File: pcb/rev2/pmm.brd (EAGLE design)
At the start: 78.6 x 43 mm, 48 parts, among them IC3 STM32F042F4, J1 AUDIO_JACK_3.5MM_PTH, J2 FFC3B07-05-T, SW4 324_SW, U2 USBC_16P, U4 XC6206_DEV

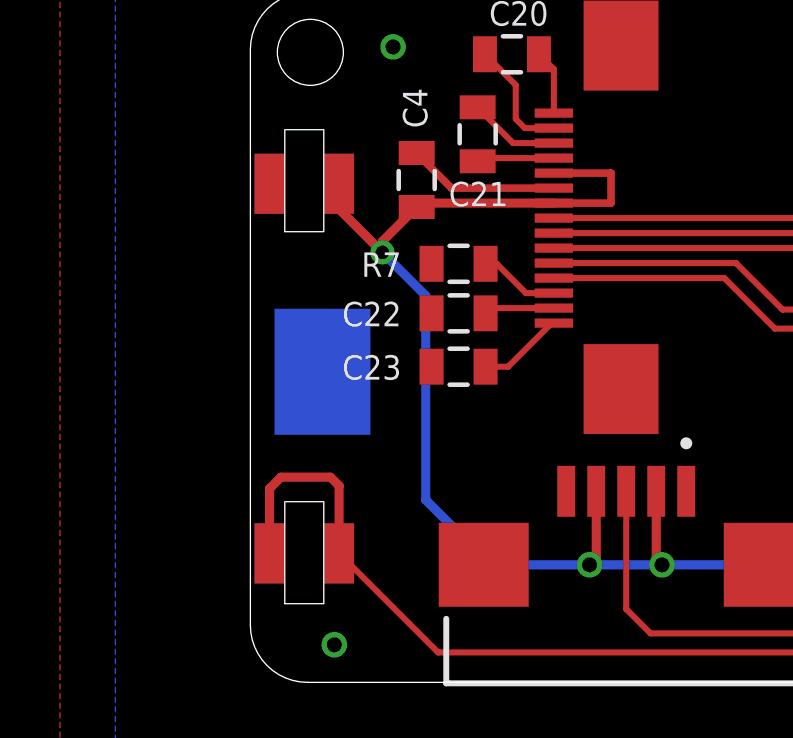
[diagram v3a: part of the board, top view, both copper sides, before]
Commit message: adjusted for pcb thickness
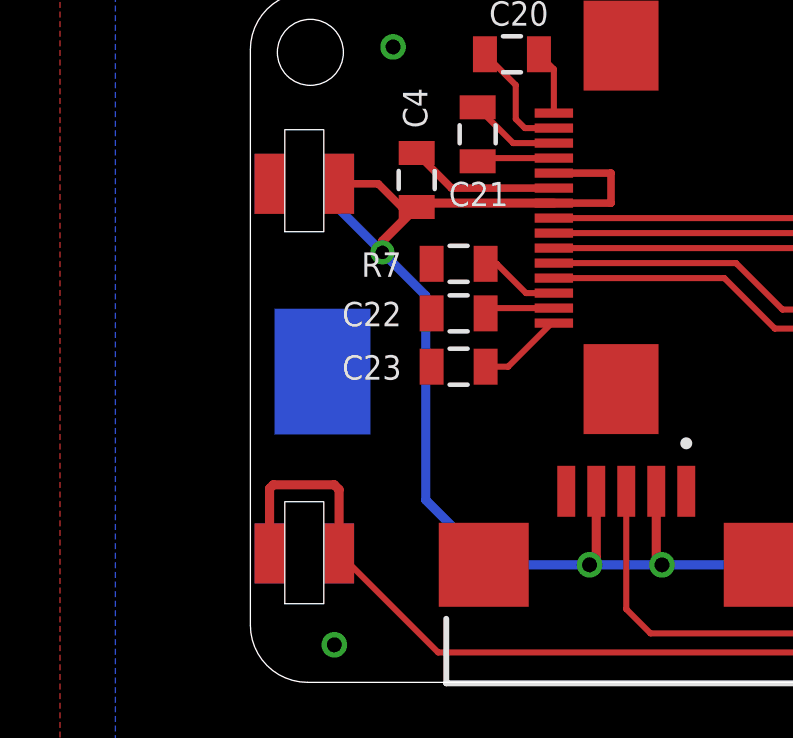
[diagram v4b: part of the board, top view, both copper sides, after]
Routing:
- net +3V3: track 143.9 -> 144.8 mm
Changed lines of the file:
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@@
 <setting verticaltext="up"/>
 </settings>
-<grid distance="10" unitdist="mil" unit="mil" style="lines" multiple="1" display="no" altdistance="1" altunitdist="mil" altunit="mil"/>
+<grid distance="5" unitdist="mil" unit="mil" style="lines" multiple="1" display="no" altdistance="1" altunitdist="mil" altunit="mil"/>
 <layers>
 <layer number="1" name="Top" color="4" fill="1" visible="yes" active="yes"/>
@@
 <layer number="19" name="Unrouted" color="6" fill="1" visible="yes" active="yes"/>
 <layer number="20" name="Dimension" color="24" fill="1" visible="yes" active="yes"/>
-<layer number="21" name="tPlace" color="7" fill="1" visible="yes" active="yes"/>
-<layer number="22" name="bPlace" color="7" fill="1" visible="yes" active="yes"/>
+<layer number="21" name="tPlace" color="7" fill="1" visible="no" active="yes"/>
+<layer number="22" name="bPlace" color="7" fill="1" visible="no" active="yes"/>
 <layer number="23" name="tOrigins" color="15" fill="1" visible="yes" active="yes"/>
 <layer number="24" name="bOrigins" color="15" fill="1" visible="yes" active="yes"/>
-<layer number="25" name="tNames" color="7" fill="1" visible="yes" active="yes"/>
-<layer number="26" name="bNames" color="7" fill="1" visible="yes" active="yes"/>
-<layer number="27" name="tValues" color="7" fill="1" visible="yes" active="yes"/>
-<layer number="28" name="bValues" color="7" fill="1" visible="yes" active="yes"/>
+<layer number="25" name="tNames" color="7" fill="1" visible="no" active="yes"/>
+<layer number="26" name="bNames" color="7" fill="1" visible="no" active="yes"/>
+<layer number="27" name="tValues" color="7" fill="1" visible="no" active="yes"/>
+<layer number="28" name="bValues" color="7" fill="1" visible="no" active="yes"/>
 <layer number="29" name="tStop" color="7" fill="3" visible="no" active="yes"/>
 <layer number="30" name="bStop" color="7" fill="6" visible="no" active="yes"/>
@@
 <layer number="49" name="Reference" color="7" fill="1" visible="no" active="yes"/>
 <layer number="50" name="dxf" color="7" fill="1" visible="no" active="no"/>
-<layer number="51" name="tDocu" color="7" fill="1" visible="yes" active="yes"/>
-<layer number="52" name="bDocu" color="7" fill="1" visible="yes" active="yes"/>
+<layer number="51" name="tDocu" color="7" fill="1" visible="no" active="yes"/>
+<layer number="52" name="bDocu" color="7" fill="1" visible="no" active="yes"/>
 <layer number="53" name="tGND_GNDA" color="7" fill="1" visible="no" active="no"/>
 <layer number="54" name="bGND_GNDA" color="7" fill="1" visible="no" active="no"/>
@@
 <text x="13.6402" y="-23.6406" size="1.016" layer="26" rot="MR0" align="center">3</text>
 <text x="17.8312" y="-21.9896" size="1.016" layer="26" rot="MR0" align="center">LS</text>
+<polygon width="0.1524" layer="41">
+<vertex x="-31.496" y="-17.907"/>
+<vertex x="-27.432" y="-17.907"/>
+<vertex x="-27.432" y="-22.733"/>
+<vertex x="-31.496" y="-22.733"/>
+</polygon>
+<polygon width="0.1524" layer="42">
+<vertex x="-31.496" y="-18.796"/>
+<vertex x="-27.559" y="-18.796"/>
+<vertex x="-27.559" y="-22.606"/>
+<vertex x="-31.496" y="-22.606"/>
+</polygon>
 </plain>
 <attributes>
@@
 <wire x1="7.771" y1="-21.844" x2="13.589" y2="-21.844" width="0.3048" layer="16"/>
 <wire x1="-28.5432" y1="-9.2238" x2="-28.5432" y2="-8.382" width="0.3048" layer="1"/>
-<wire x1="-27.099" y1="-10.668" x2="-28.5432" y2="-9.2238" width="0.3048" layer="1"/>
 <wire x1="-27.099" y1="-10.668" x2="-27.099" y2="-10.298" width="0.3048" layer="1"/>
 <wire x1="-27.099" y1="-10.298" x2="-25.956" y2="-9.155" width="0.3048" layer="1"/>
 <wire x1="-28.5432" y1="-8.382" x2="-28.5432" y2="-9.2238" width="0.3048" layer="16"/>
 <wire x1="-28.5432" y1="-9.2238" x2="-27.099" y2="-10.668" width="0.3048" layer="16"/>
+<wire x1="-25.956" y1="-9.155" x2="-26.464" y2="-9.155" width="0.254" layer="1"/>
+<wire x1="-26.464" y1="-9.155" x2="-27.237" y2="-8.382" width="0.254" layer="1"/>
+<wire x1="-27.237" y1="-8.382" x2="-28.5432" y2="-8.382" width="0.254" layer="1"/>
 </signal>
 <signal name="USB_DP">
@@
 <wire x1="19.05" y1="-23.241" x2="20.447" y2="-21.844" width="0.2032" layer="1"/>
 <wire x1="-30.861" y1="-20.701" x2="-30.861" y2="-18.542" width="0.3048" layer="1"/>
-<wire x1="-30.861" y1="-18.542" x2="-30.48" y2="-18.161" width="0.3048" layer="1"/>
-<wire x1="-30.48" y1="-18.161" x2="-28.829" y2="-18.161" width="0.3048" layer="1"/>
-<wire x1="-28.5432" y1="-18.4468" x2="-28.5432" y2="-20.701" width="0.3048" layer="1"/>
-<wire x1="-28.829" y1="-18.161" x2="-28.5432" y2="-18.4468" width="0.3048" layer="1"/>
+<wire x1="-30.861" y1="-18.542" x2="-30.734" y2="-18.415" width="0.3048" layer="1"/>
+<wire x1="-30.734" y1="-18.415" x2="-28.702" y2="-18.415" width="0.3048" layer="1"/>
+<wire x1="-28.5432" y1="-18.5738" x2="-28.5432" y2="-20.701" width="0.3048" layer="1"/>
+<wire x1="-28.702" y1="-18.415" x2="-28.5432" y2="-18.5738" width="0.3048" layer="1"/>
 <wire x1="-25.2412" y1="-24.003" x2="-28.5432" y2="-20.701" width="0.2032" layer="1"/>
 <wire x1="-1.651" y1="-24.003" x2="-25.2412" y2="-24.003" width="0.2032" layer="1"/>

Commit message: reset button
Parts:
- added SW3: 324_SW324_SWITCH_FOOT_HOLE, 3pos_slide_switch:342_SWICH_FOOT_HOLE
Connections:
- removed net BUTTON1: IC3.4
- new net RESET: IC3.4, SW3.P$1, SW3.P$4
- net GND: now also SW3.P$2, SW3.P$3
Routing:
- net RESET: track 0.00 -> 14.7 mm, vias 0 -> 1
- net +3V3: track 144.8 -> 143.8 mm
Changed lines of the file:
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@@
 <layer number="19" name="Unrouted" color="6" fill="1" visible="yes" active="yes"/>
 <layer number="20" name="Dimension" color="24" fill="1" visible="yes" active="yes"/>
-<layer number="21" name="tPlace" color="7" fill="1" visible="no" active="yes"/>
-<layer number="22" name="bPlace" color="7" fill="1" visible="no" active="yes"/>
+<layer number="21" name="tPlace" color="7" fill="1" visible="yes" active="yes"/>
+<layer number="22" name="bPlace" color="7" fill="1" visible="yes" active="yes"/>
 <layer number="23" name="tOrigins" color="15" fill="1" visible="yes" active="yes"/>
 <layer number="24" name="bOrigins" color="15" fill="1" visible="yes" active="yes"/>
-<layer number="25" name="tNames" color="7" fill="1" visible="no" active="yes"/>
-<layer number="26" name="bNames" color="7" fill="1" visible="no" active="yes"/>
-<layer number="27" name="tValues" color="7" fill="1" visible="no" active="yes"/>
-<layer number="28" name="bValues" color="7" fill="1" visible="no" active="yes"/>
+<layer number="25" name="tNames" color="7" fill="1" visible="yes" active="yes"/>
+<layer number="26" name="bNames" color="7" fill="1" visible="yes" active="yes"/>
+<layer number="27" name="tValues" color="7" fill="1" visible="yes" active="yes"/>
+<layer number="28" name="bValues" color="7" fill="1" visible="yes" active="yes"/>
 <layer number="29" name="tStop" color="7" fill="3" visible="no" active="yes"/>
 <layer number="30" name="bStop" color="7" fill="6" visible="no" active="yes"/>
@@
 <layer number="42" name="bRestrict" color="1" fill="10" visible="yes" active="yes"/>
 <layer number="43" name="vRestrict" color="2" fill="10" visible="no" active="yes"/>
-<layer number="44" name="Drills" color="7" fill="1" visible="no" active="yes"/>
-<layer number="45" name="Holes" color="7" fill="1" visible="no" active="yes"/>
+<layer number="44" name="Drills" color="7" fill="1" visible="yes" active="yes"/>
+<layer number="45" name="Holes" color="7" fill="1" visible="yes" active="yes"/>
 <layer number="46" name="Milling" color="3" fill="1" visible="yes" active="yes"/>
 <layer number="47" name="Measures" color="7" fill="1" visible="no" active="yes"/>
@@
 <layer number="49" name="Reference" color="7" fill="1" visible="no" active="yes"/>
 <layer number="50" name="dxf" color="7" fill="1" visible="no" active="no"/>
-<layer number="51" name="tDocu" color="7" fill="1" visible="no" active="yes"/>
-<layer number="52" name="bDocu" color="7" fill="1" visible="no" active="yes"/>
+<layer number="51" name="tDocu" color="7" fill="1" visible="yes" active="yes"/>
+<layer number="52" name="bDocu" color="7" fill="1" visible="yes" active="yes"/>
 <layer number="53" name="tGND_GNDA" color="7" fill="1" visible="no" active="no"/>
 <layer number="54" name="bGND_GNDA" color="7" fill="1" visible="no" active="no"/>
@@
 <layer number="154" name="FabDoc2" color="7" fill="1" visible="no" active="yes"/>
 <layer number="155" name="FabDoc3" color="7" fill="1" visible="no" active="yes"/>
+<layer number="156" name="gesam-Maß" color="7" fill="1" visible="no" active="yes"/>
+<layer number="157" name="FaceMchng" color="7" fill="1" visible="no" active="yes"/>
+<layer number="158" name="FaceMMeas" color="7" fill="1" visible="no" active="yes"/>
+<layer number="159" name="Geh-Bear2" color="7" fill="1" visible="no" active="yes"/>
+<layer number="160" name="O_Dim" color="7" fill="1" visible="no" active="yes"/>
+<layer number="161" name="tomplace2" color="7" fill="1" visible="no" active="yes"/>
 <layer number="166" name="AntennaArea" color="7" fill="1" visible="no" active="yes"/>
 <layer number="168" name="4mmHeightArea" color="7" fill="1" visible="no" active="yes"/>
@@
 <layer number="250" name="Descript" color="3" fill="1" visible="no" active="no"/>
 <layer number="251" name="SMDround" color="12" fill="11" visible="no" active="no"/>
+<layer number="252" name="BR-BS" color="7" fill="1" visible="no" active="yes"/>
 <layer number="253" name="Extra" color="7" fill="1" visible="no" active="yes"/>
 <layer number="254" name="cooling" color="7" fill="1" visible="no" active="yes"/>
@@
 <text x="4.953" y="0.889" size="1.27" layer="25" rot="R270" align="center">HSHOE</text>
 <text x="2.3944" y="-0.1782" size="1.27" layer="25" rot="R270" align="center">GND</text>
-<text x="-5.6638" y="-23.5136" size="1.9304" layer="25" align="center">USER</text>
+<text x="-5.8" y="-23.5136" size="1.9304" layer="25" align="center">USER</text>
 <text x="2.667" y="-17.78" size="2.1844" layer="25" align="center">ON</text>
 <text x="10.033" y="-17.78" size="2.1844" layer="25" align="center">OFF</text>
@@
 <attribute name="TP_SIGNAL_NAME" value="" x="15.367" y="-23.622" size="1.778" layer="28" rot="MR0" display="off"/>
 </element>
+<element name="SW3" library="3pos_slide_switch" package="342_SWICH_FOOT_HOLE" value="324_SW324_SWITCH_FOOT_HOLE" x="31.877" y="-23.368" smashed="yes" rot="MR180"/>
 </elements>
 <signals>
@@
 <via x="-28.702" y="-23.749" extent="1-16" drill="0.5"/>
 <contactref element="TP2" pad="TP"/>
+<contactref element="SW3" pad="P$3"/>
+<contactref element="SW3" pad="P$2"/>
 </signal>
 <signal name="+3V3">
@@
 <contactref element="R6" pad="2"/>
 <wire x1="28.25" y1="-15.8718" x2="28.25" y2="-17.343" width="0.1524" layer="1"/>
-<wire x1="27.9654" y1="-17.6276" x2="27.9654" y2="-20.193" width="0.1524" layer="1"/>
-<wire x1="27.9654" y1="-20.193" x2="28.3464" y2="-20.574" width="0.1524" layer="1"/>
-<wire x1="28.3464" y1="-20.574" x2="29.718" y2="-20.574" width="0.1524" layer="1"/>
+<wire x1="27.9654" y1="-17.6276" x2="27.9654" y2="-19.939" width="0.1524" layer="1"/>
+<wire x1="27.9654" y1="-19.939" x2="28.6004" y2="-20.574" width="0.1524" layer="1"/>
+<wire x1="28.6004" y1="-20.574" x2="29.718" y2="-20.574" width="0.1524" layer="1"/>
 <wire x1="29.718" y1="-20.574" x2="30.353" y2="-19.939" width="0.1524" layer="1"/>
 <wire x1="30.353" y1="-19.939" x2="30.353" y2="-18.923" width="0.1524" layer="1"/>
@@
 <wire x1="13.589" y1="-21.844" x2="15.367" y2="-23.622" width="0.3048" layer="16"/>
 <wire x1="7.771" y1="-21.844" x2="13.589" y2="-21.844" width="0.3048" layer="16"/>
-<wire x1="-28.5432" y1="-9.2238" x2="-28.5432" y2="-8.382" width="0.3048" layer="1"/>
 <wire x1="-27.099" y1="-10.668" x2="-27.099" y2="-10.298" width="0.3048" layer="1"/>
 <wire x1="-27.099" y1="-10.298" x2="-25.956" y2="-9.155" width="0.3048" layer="1"/>
@@
 <wire x1="35.036" y1="-19.966" x2="35.063" y2="-19.939" width="0.3048" layer="1"/>
 </signal>
-<signal name="BUTTON1">
+<signal name="RESET">
 <contactref element="IC3" pad="4"/>
+<contactref element="SW3" pad="P$1"/>
+<contactref element="SW3" pad="P$4"/>
+<wire x1="27.6" y1="-15.8718" x2="27.6" y2="-20.234" width="0.1524" layer="1"/>
+<wire x1="28.829" y1="-21.463" x2="30.988" y2="-21.463" width="0.1524" layer="1"/>
+<via x="30.988" y="-21.463" extent="1-16" drill="0.5"/>
+<wire x1="29.908" y1="-22.543" x2="29.845" y2="-22.543" width="0.1524" layer="16"/>
+<wire x1="29.845" y1="-22.543" x2="29.827" y2="-22.543" width="0.1524" layer="16"/>
+<wire x1="27.6" y1="-20.234" x2="28.829" y2="-21.463" width="0.1524" layer="1"/>
+<wire x1="33.927" y1="-22.543" x2="33.102" y2="-23.368" width="0.1524" layer="16"/>
+<wire x1="30.67" y1="-23.368" x2="29.845" y2="-22.543" width="0.1524" layer="16"/>
+<wire x1="33.102" y1="-23.368" x2="30.67" y2="-23.368" width="0.1524" layer="16"/>
+<wire x1="30.988" y1="-21.463" x2="29.908" y2="-22.543" width="0.2032" layer="16"/>
+<wire x1="29.908" y1="-22.543" x2="29.827" y2="-22.543" width="0.2032" layer="16"/>
 </signal>
 <signal name="BUTTON2">
@@
 <contactref element="U4" pad="2"/>
 <contactref element="JP1" pad="3"/>
-<wire x1="33.036" y1="-23.81" x2="30.541" y2="-23.81" width="0.3048" layer="1"/>
-<wire x1="30.541" y1="-23.81" x2="25.4" y2="-18.669" width="0.3048" layer="1"/>
-<wire x1="25.4" y1="-18.669" x2="19.812" y2="-18.669" width="0.3048" layer="1"/>
+<wire x1="33.036" y1="-23.81" x2="32.5534" y2="-23.3274" width="0.3048" layer="1"/>
+<wire x1="32.5534" y1="-23.3274" x2="29.8044" y2="-23.3274" width="0.3048" layer="1"/>
+<wire x1="29.8044" y1="-23.3274" x2="25.146" y2="-18.669" width="0.3048" layer="1"/>
+<wire x1="25.146" y1="-18.669" x2="19.812" y2="-18.669" width="0.3048" layer="1"/>
 <wire x1="19.812" y1="-18.669" x2="19.177" y2="-19.304" width="0.3048" layer="1"/>
 <wire x1="19.177" y1="-19.304" x2="19.177" y2="-21.463" width="0.3048" layer="1"/>
